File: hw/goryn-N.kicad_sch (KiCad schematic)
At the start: 4 parts, among them J4 Conn_01x34

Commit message: added DC-DC
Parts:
- added C13: 22uF, AI6YP:C_0603_1608Metric, symbol AI6YP:C
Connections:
- net +3V3: now also C13.1
- net GND: now also C13.2
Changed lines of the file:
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@@
+    (stroke (width 0) (type default))
+  )
+  (wire (pts (xy 137 49) (xy 137 51))
     (stroke (width 0) (type default))
   )
@@
   )
   (wire (pts (xy 126 154) (xy 117 154))
+    (stroke (width 0) (type default))
+  )
+  (wire (pts (xy 137 44) (xy 137 47))
     (stroke (width 0) (type default))
   )
@@
         (path "/745fe258-3c32-4527-ad01-ef9d3fd5a8f9/efafad0f-667d-4481-b30a-d8d0ba7927b3"
           (reference "#PWR072") (unit 1)
+        )
+      )
+    )
+  )
+  (symbol (lib_id "AI6YP:C") (at 137 48 0) (unit 1)
+    (in_bom yes) (on_board yes) (dnp no)
+    (property "Reference" "C13" (at 138 47 0)
+      (effects (font (size 1 1)) (justify left))
+    )
+    (property "Value" "22uF" (at 138 49 0)
+      (effects (font (size 1 1)) (justify left))
+    )
+    (property "Footprint" "AI6YP:C_0603_1608Metric" (at 138 52 0)
+      (effects (font (size 1 1)) hide)
+    )
+    (property "Datasheet" "~" (at 137 48 0)
+      (effects (font (size 1 1)) hide)
+    )
+    (pin "1")
+    (pin "2")
+    (instances
+      (project "goryn"
+        (path "/745fe258-3c32-4527-ad01-ef9d3fd5a8f9/efafad0f-667d-4481-b30a-d8d0ba7927b3"
+          (reference "C13") (unit 1)
         )
       )
@@
     )
   )
+  (symbol (lib_id "AI6YP:+3V3") (at 137 44 0) (unit 1)
+    (in_bom yes) (on_board yes) (dnp no) (fields_autoplaced)
+    (property "Reference" "#PWR0111" (at 137 46 0)
+      (effects (font (size 1 1)) hide)
+    )
+    (property "Value" "+3V3" (at 137 40.28 0)
+      (effects (font (size 1 1)))
+    )
+    (property "Footprint" "" (at 137 44 0)
+      (effects (font (size 1 1)) hide)
+    )
+    (property "Datasheet" "" (at 137 44 0)
+      (effects (font (size 1 1)) hide)
+    )
+    (pin "1")
+    (instances
+      (project "goryn"
+        (path "/745fe258-3c32-4527-ad01-ef9d3fd5a8f9/efafad0f-667d-4481-b30a-d8d0ba7927b3"
+          (reference "#PWR0111") (unit 1)
+        )
+      )
+    )
+  )
   (symbol (lib_id "AI6YP:GND") (at 154 220 270) (unit 1)
     (in_bom yes) (on_board yes) (dnp no) (fields_autoplaced)
@@
         )
       )
+    )
+  )
+  (symbol (lib_id "AI6YP:GND") (at 137 51 0) (unit 1)
+    (in_bom yes) (on_board yes) (dnp no) (fields_autoplaced)
+    (property "Reference" "#PWR0112" (at 137 55 0)
+      (effects (font (size 1 1)) hide)
+    )
+    (property "Value" "GND" (at 137 54.22 0)
+      (effects (font (size 1 1)))
+    )
+    (property "Footprint" "" (at 137 51 0)
+      (effects (font (size 1 1)) hide)
+    )
+    (property "Datasheet" "" (at 137 51 0)
+      (effects (font (size 1 1)) hide)
+    )
+    (pin "1")
+    (instances
+      (project "goryn"
+        (path "/745fe258-3c32-4527-ad01-ef9d3fd5a8f9/efafad0f-667d-4481-b30a-d8d0ba7927b3"
+          (reference "#PWR0112") (unit 1)
+        )
+      )

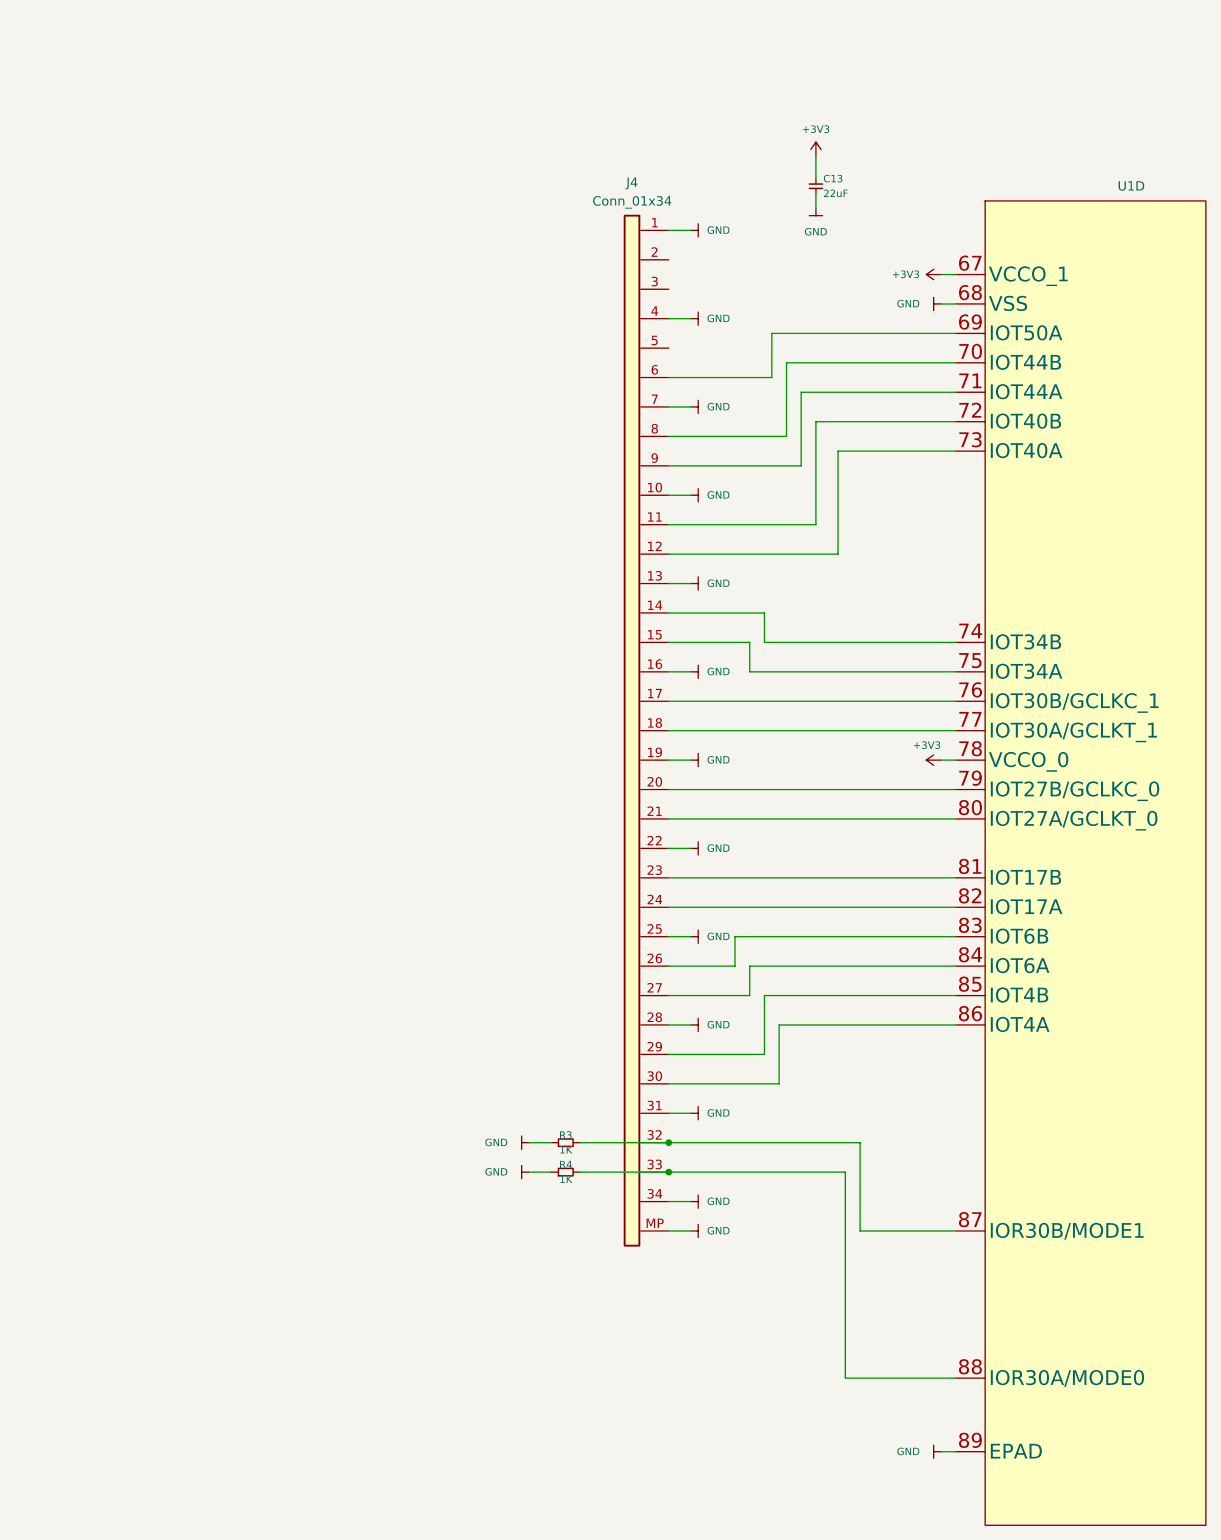
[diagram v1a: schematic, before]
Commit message: FFC34 -> FFC30
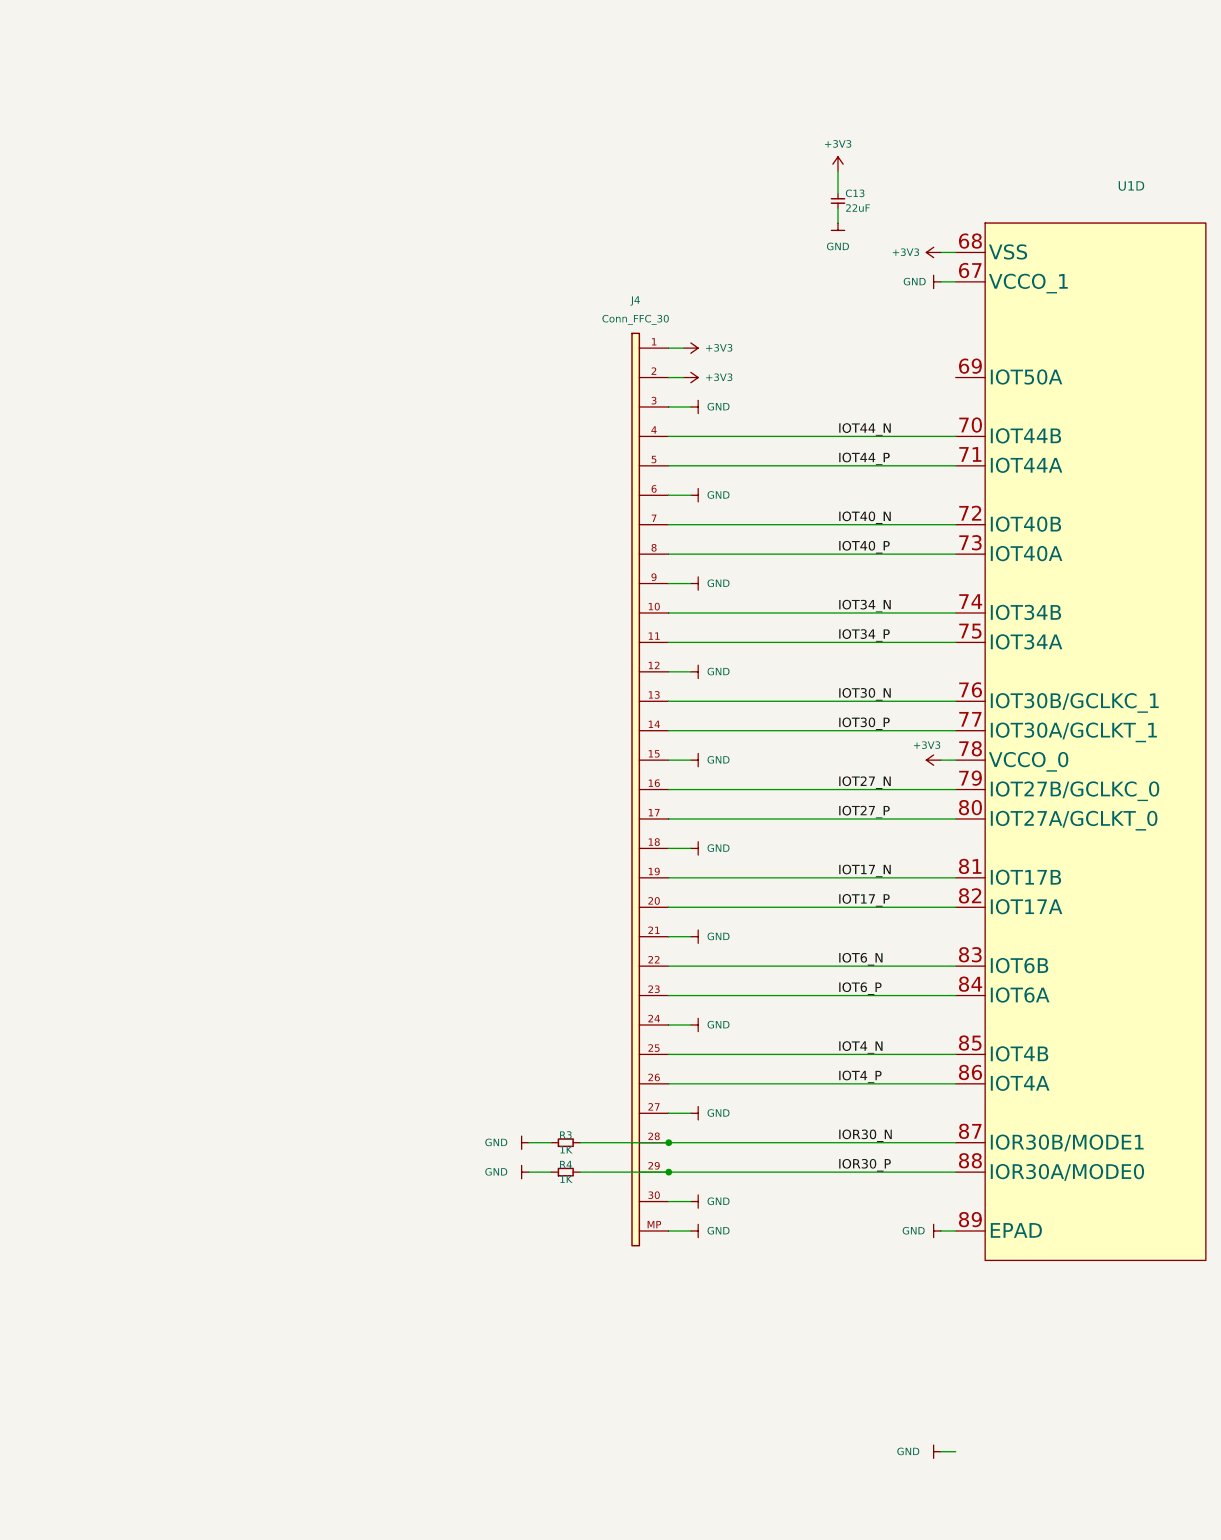
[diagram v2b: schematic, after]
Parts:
- removed J4: Conn_01x34, AI6YP:Hirose_FH12-34S-0.5SH_1x34-1MP_P0.50mm_Horizontal, symbol AI6YP:Conn_01x34
- added J4: Conn_FFC_30, AI6YP:Hirose_FH12-30S-0.5SH_1x30-1MP_P0.50mm_Horizontal, symbol AI6YP:Conn_FFC_30
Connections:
- net +3V3: now also U1.68 (VSS), J4.1 (Pin_1), J4.2 (Pin_2); no longer U1.67 (VCCO_1)
- net GND: now also U1.67 (VCCO_1), J4.12 (Pin_12), J4.15 (Pin_15), J4.18 (Pin_18), J4.21 (Pin_21), J4.24 (Pin_24), J4.27 (Pin_27), J4.3 (Pin_3), J4.30 (Pin_30), J4.6 (Pin_6), J4.9 (Pin_9), J4.MP (Pin_MP); no longer U1.68 (VSS)
- net IOT44_N: now reaches U1.70 (IOT44B)
- net IOT44_N: now also J4.4 (Pin_4)
- net IOT44_P: now reaches U1.71 (IOT44A)
- net IOT44_P: now also J4.5 (Pin_5)
- net IOT40_N: now reaches U1.72 (IOT40B)
- net IOT40_N: now also J4.7 (Pin_7)
- net IOT40_P: now reaches U1.73 (IOT40A)
- net IOT40_P: now also J4.8 (Pin_8)
- net IOT34_N: now reaches U1.74 (IOT34B)
- net IOT34_N: now also J4.10 (Pin_10)
- net IOT34_P: now reaches U1.75 (IOT34A)
- net IOT34_P: now also J4.11 (Pin_11)
- net IOT30_N: now reaches U1.76 (IOT30B/GCLKC_1)
- net IOT30_N: now also J4.13 (Pin_13)
- net IOT30_P: now reaches U1.77 (IOT30A/GCLKT_1)
- net IOT30_P: now also J4.14 (Pin_14)
- net IOT27_N: now reaches U1.79 (IOT27B/GCLKC_0)
- net IOT27_N: now also J4.16 (Pin_16)
- net IOT27_P: now reaches U1.80 (IOT27A/GCLKT_0)
- net IOT27_P: now also J4.17 (Pin_17)
- net IOT17_N: now reaches U1.81 (IOT17B)
- net IOT17_N: now also J4.19 (Pin_19)
- net IOT17_P: now reaches U1.82 (IOT17A)
- net IOT17_P: now also J4.20 (Pin_20)
- net IOT6_N: now reaches U1.83 (IOT6B)
- net IOT6_N: now also J4.22 (Pin_22)
- net IOT6_P: now reaches U1.84 (IOT6A)
- net IOT6_P: now also J4.23 (Pin_23)
- net IOT4_N: now reaches U1.85 (IOT4B)
- net IOT4_N: now also J4.25 (Pin_25)
- net IOT4_P: now reaches U1.86 (IOT4A)
- net IOT4_P: now also J4.26 (Pin_26)
- net IOR30_N: now reaches R3.2, U1.87 (IOR30B/MODE1)
- net IOR30_N: now also J4.28 (Pin_28)
- net IOR30_P: now reaches R4.2, U1.88 (IOR30A/MODE0)
- net IOR30_P: now also J4.29 (Pin_29)
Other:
- moved on the sheet: U1D

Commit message: happy kicad 8
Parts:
- added H4: MountingHole_M3, AI6YP:MountingHole_3.2mm_M3_Pad_Via, symbol AI6YP:MountingHole_M3
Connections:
- net +3V3: now also J4.30 (Pin_30), U1.67 (VCCO_1); no longer J4.2 (Pin_2), U1.68 (VSS)
- net GND: now also J4.11 (Pin_11), J4.14 (Pin_14), J4.17 (Pin_17), J4.2 (Pin_2), J4.20 (Pin_20), J4.23 (Pin_23), J4.26 (Pin_26), J4.29 (Pin_29), J4.5 (Pin_5), J4.8 (Pin_8), U1.68 (VSS), H4.1; no longer J4.12 (Pin_12), J4.15 (Pin_15), J4.18 (Pin_18), J4.21 (Pin_21), J4.24 (Pin_24), J4.27 (Pin_27), J4.3 (Pin_3), J4.30 (Pin_30), J4.6 (Pin_6), J4.9 (Pin_9), U1.67 (VCCO_1)
- net IOR30_N: now also J4.27 (Pin_27); no longer J4.28 (Pin_28)
- net IOR30_P: now also J4.28 (Pin_28); no longer J4.29 (Pin_29)
- net IOT17_N: now also J4.18 (Pin_18); no longer J4.19 (Pin_19)
- net IOT17_P: now also J4.19 (Pin_19); no longer J4.20 (Pin_20)
- net IOT27_N: now also J4.15 (Pin_15); no longer J4.16 (Pin_16)
- net IOT27_P: now also J4.16 (Pin_16); no longer J4.17 (Pin_17)
- net IOT30_N: now also J4.12 (Pin_12); no longer J4.13 (Pin_13)
- net IOT30_P: now also J4.13 (Pin_13); no longer J4.14 (Pin_14)
- net IOT34_N: now also J4.9 (Pin_9); no longer J4.10 (Pin_10)
- net IOT34_P: now also J4.10 (Pin_10); no longer J4.11 (Pin_11)
- net IOT40_N: now also J4.6 (Pin_6); no longer J4.7 (Pin_7)
- net IOT40_P: now also J4.7 (Pin_7); no longer J4.8 (Pin_8)
- net IOT44_N: now also J4.3 (Pin_3); no longer J4.4 (Pin_4)
- net IOT44_P: now also J4.4 (Pin_4); no longer J4.5 (Pin_5)
- net IOT4_N: now also J4.24 (Pin_24); no longer J4.25 (Pin_25)
- net IOT4_P: now also J4.25 (Pin_25); no longer J4.26 (Pin_26)
- net IOT6_N: now also J4.21 (Pin_21); no longer J4.22 (Pin_22)
- net IOT6_P: now also J4.22 (Pin_22); no longer J4.23 (Pin_23)
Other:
- moved on the sheet: C13, J4, R3, R4, U1D

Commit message: finished routing
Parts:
- removed H4: MountingHole_M3, AI6YP:MountingHole_3.2mm_M3_Pad_Via, symbol AI6YP:MountingHole_M3
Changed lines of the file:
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@@
 	(wire
 		(pts
-			(xy 30 33) (xy 30 35)
+			(xy 57 156) (xy 69 156)
 		)
 		(stroke
@@
 	(wire
 		(pts
-			(xy 57 156) (xy 69 156)
+			(xy 69 68) (xy 72 68)
 		)
 		(stroke
@@
 		)
 	)
-	(wire
-		(pts
-			(xy 69 68) (xy 72 68)
-		)
-		(stroke
-			(width 0)
-			(type default)
-		)
-	)
 	(label "IOR30_N"
 		(at 92 156 0)
@@
 			)
 		)
-		(property "Description" ""
+		(property "Description" "Power symbol creates a global label with name \"GND\" , ground"
 			(at 72 164 0)
 			(effects
@@
 			)
 		)
-		(property "Description" ""
+		(property "Description" "Power symbol creates a global label with name \"+3V3\""
 			(at 106 40 0)
 			(effects
@@
 			)
 		)
-		(property "Description" ""
+		(property "Description" "Power symbol creates a global label with name \"GND\" , ground"
 			(at 50 156 0)
 			(effects
@@
 			)
 		)
-		(property "Description" ""
+		(property "Description" "Power symbol creates a global label with name \"GND\" , ground"
 			(at 72 140 0)
 			(effects
@@
 			)
 		)
-		(property "Description" ""
+		(property "Description" "Power symbol creates a global label with name \"GND\" , ground"
 			(at 72 68 0)
 			(effects
@@
 			)
 		)
-		(property "Description" ""
+		(property "Description" "Power symbol creates a global label with name \"GND\" , ground"
 			(at 72 104 0)
 			(effects
@@
 			)
 		)
-		(property "Description" ""
+		(property "Description" "Power symbol creates a global label with name \"GND\" , ground"
 			(at 72 116 0)
 			(effects
@@
 				(path "/745fe258-3c32-4527-ad01-ef9d3fd5a8f9/efafad0f-667d-4481-b30a-d8d0ba7927b3"
 					(reference "#PWR069")
-					(unit 1)
-				)
-			)
-		)
-	)
-	(symbol
-		(lib_id "AI6YP:MountingHole_M3")
-		(at 30 30 0)
-		(unit 1)
-		(exclude_from_sim no)
-		(in_bom yes)
-		(on_board yes)
-		(dnp no)
-		(fields_autoplaced yes)
-		(property "Reference" "H4"
-			(at 33.02 27.46 0)
-			(effects
-				(font
-					(size 1.27 1.27)
-				)
-				(justify left)
-			)
-		)
-		(property "Value" "MountingHole_M3"
-			(at 33.02 30 0)
-			(effects
-				(font
-					(size 1.27 1.27)
-				)
-				(justify left)
-			)
-		)
-		(property "Footprint" "AI6YP:MountingHole_3.2mm_M3_Pad_Via"
-			(at 30 30 0)
-			(effects
-				(font
-					(size 1.27 1.27)
-				)
-				(hide yes)
-			)
-		)
-		(property "Datasheet" "~"
-			(at 30 30 0)
-			(effects
-				(font
-					(size 1.27 1.27)
-				)
-				(hide yes)
-			)
-		)
-		(property "Description" ""
-			(at 30 30 0)
-			(effects
-				(font
-					(size 1.27 1.27)
-				)
-				(hide yes)
-			)
-		)
-		(pin "1"
-		)
-		(instances
-			(project "goryn"
-				(path "/745fe258-3c32-4527-ad01-ef9d3fd5a8f9/efafad0f-667d-4481-b30a-d8d0ba7927b3"
-					(reference "H4")
 					(unit 1)
 				)
@@
 			)
 		)
-		(property "Description" ""
+		(property "Description" "Power symbol creates a global label with name \"GND\" , ground"
 			(at 72 152 0)
 			(effects
@@
 			)
 		)
-		(property "Description" ""
+		(property "Description" "Unpolarized capacitor"
 			(at 90 36 0)
 			(effects
@@
 			)
 		)
-		(property "Description" ""
+		(property "Description" "Power symbol creates a global label with name \"+3V3\""
 			(at 71 168 0)
 			(effects
@@
 			)
 		)
-		(property "Description" ""
+		(property "Description" "Power symbol creates a global label with name \"GND\" , ground"
 			(at 90 39 0)
 			(effects
@@
 			)
 		)
-		(property "Description" ""
+		(property "Description" "FFC 30 pin connector"
 			(at 84 112 0)
 			(effects
@@
 			)
 		)
-		(property "Description" ""
+		(property "Description" "Power symbol creates a global label with name \"GND\" , ground"
 			(at 72 172 0)
 			(effects
@@
 			)
 		)
-		(property "Description" ""
+		(property "Description" "Power symbol creates a global label with name \"+3V3\""
 			(at 71 52 0)
 			(effects
@@
 			)
 		)
-		(property "Description" ""
+		(property "Description" "Power symbol creates a global label with name \"GND\" , ground"
 			(at 72 56 0)
 			(effects
@@
 			)
 		)
-		(property "Description" ""
+		(property "Description" "Power symbol creates a global label with name \"+3V3\""
 			(at 106 104 0)
 			(effects
@@
 			)
 		)
-		(property "Description" ""
+		(property "Description" "Resistor"
 			(at 55 160 0)
 			(effects
@@
 			)
 		)
-		(property "Description" ""
+		(property "Description" "Power symbol creates a global label with name \"GND\" , ground"
 			(at 72 128 0)
 			(effects
@@
 			)
 		)
-		(property "Description" ""
+		(property "Description" "Power symbol creates a global label with name \"GND\" , ground"
 			(at 72 80 0)
 			(effects
@@
 			)
 		)
-		(property "Description" ""
+		(property "Description" "Power symbol creates a global label with name \"GND\" , ground"
 			(at 106 168 0)
 			(effects
@@
 			)
 		)
-		(property "Description" ""
+		(property "Description" "Resistor"
 			(at 55 156 0)
 			(effects
@@
 				(path "/745fe258-3c32-4527-ad01-ef9d3fd5a8f9/efafad0f-667d-4481-b30a-d8d0ba7927b3"
 					(reference "R3")
-					(unit 1)
-				)
-			)
-		)
-	)
-	(symbol
-		(lib_id "AI6YP:GND")
-		(at 30 35 0)
-		(unit 1)
-		(exclude_from_sim no)
-		(in_bom yes)
-		(on_board yes)
-		(dnp no)
-		(fields_autoplaced yes)
-		(property "Reference" "#PWR033"
-			(at 30 39 0)
-			(effects
-				(font
-					(size 1 1)
-				)
-				(hide yes)
-			)
-		)
-		(property "Value" "GND"
-			(at 30 38.22 0)
-			(effects
-				(font
-					(size 1 1)
-				)
-			)
-		)
-		(property "Footprint" ""
-			(at 30 35 0)
-			(effects
-				(font
-					(size 1 1)
-				)
-				(hide yes)
-			)
-		)
-		(property "Datasheet" ""
-			(at 30 35 0)
-			(effects
-				(font
-					(size 1 1)
-				)
-				(hide yes)
-			)
-		)
-		(property "Description" ""
-			(at 30 35 0)
-			(effects
-				(font
-					(size 1.27 1.27)
-				)
-				(hide yes)
-			)
-		)
-		(pin "1"
-		)
-		(instances
-			(project "goryn"
-				(path "/745fe258-3c32-4527-ad01-ef9d3fd5a8f9/efafad0f-667d-4481-b30a-d8d0ba7927b3"
-					(reference "#PWR033")
 					(unit 1)
 				)
@@
 			)
 		)
-		(property "Description" ""
+		(property "Description" "Power symbol creates a global label with name \"GND\" , ground"
 			(at 106 44 0)
 			(effects
@@
 			)
 		)
-		(property "Description" ""
+		(property "Description" "Power symbol creates a global label with name \"+3V3\""
 			(at 90 32 0)
 			(effects
@@
 			)
 		)
-		(property "Description" ""
+		(property "Description" "Power symbol creates a global label with name \"GND\" , ground"
 			(at 72 92 0)
 			(effects
@@
 			)
 		)
-		(property "Description" ""
+		(property "Description" "Power symbol creates a global label with name \"GND\" , ground"
 			(at 50 160 0)
 			(effects

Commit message: v1.0.0
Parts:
- U1: footprint AI6YP:QFN-88-10x10mm-P0.4mm-EP6.74x6.74mm -> AI6YP:GIWIN-QFN-88-10x10mm-P0.4mm-EP6.74x6.74mm
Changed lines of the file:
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@@
 			)
 		)
-		(property "Footprint" "AI6YP:QFN-88-10x10mm-P0.4mm-EP6.74x6.74mm"
+		(property "Footprint" "AI6YP:GIWIN-QFN-88-10x10mm-P0.4mm-EP6.74x6.74mm"
 			(at 112 38 0)
 			(effects
